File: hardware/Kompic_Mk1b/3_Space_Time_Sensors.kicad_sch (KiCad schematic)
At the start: 37 parts, among them CN1 Qvar_Electrode_2, U5 LSM6DSV16XTR, U6 MAX-M10S-00B, U7 LIS3MDLTR, U8 PCF85063ATL/1,118, X1 FC31M2-32.768-NTLLLDT

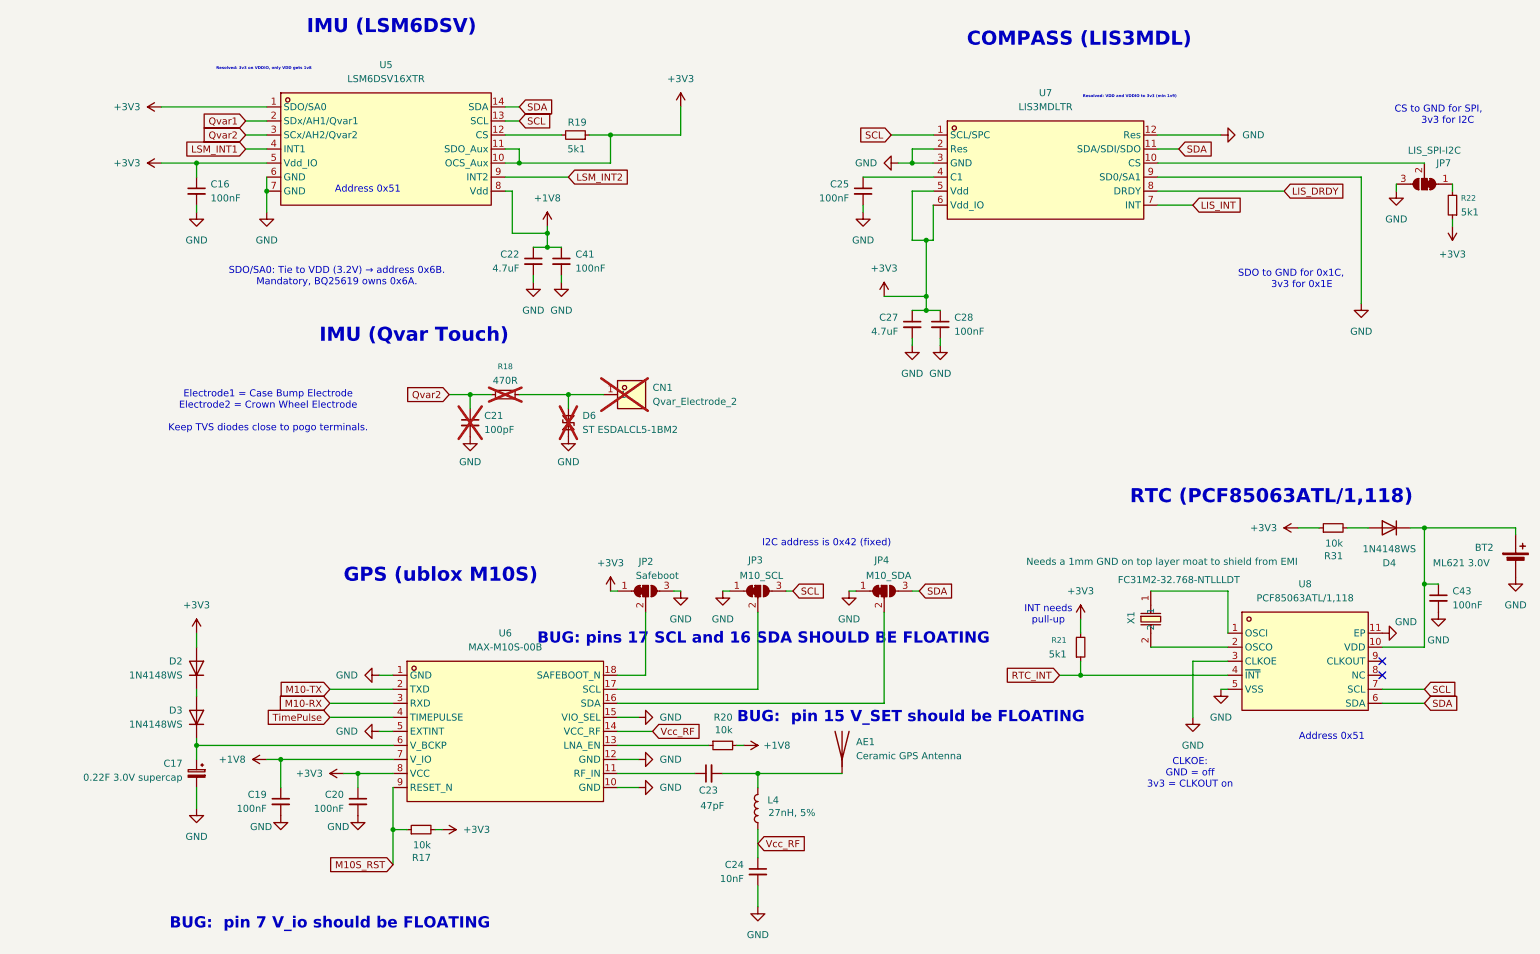
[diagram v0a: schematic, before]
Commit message: Final firmware changes; GPS hardware fixing and arduino sketches (18, 19); Started progress on migrating to LVGL 9 optimized architecture.
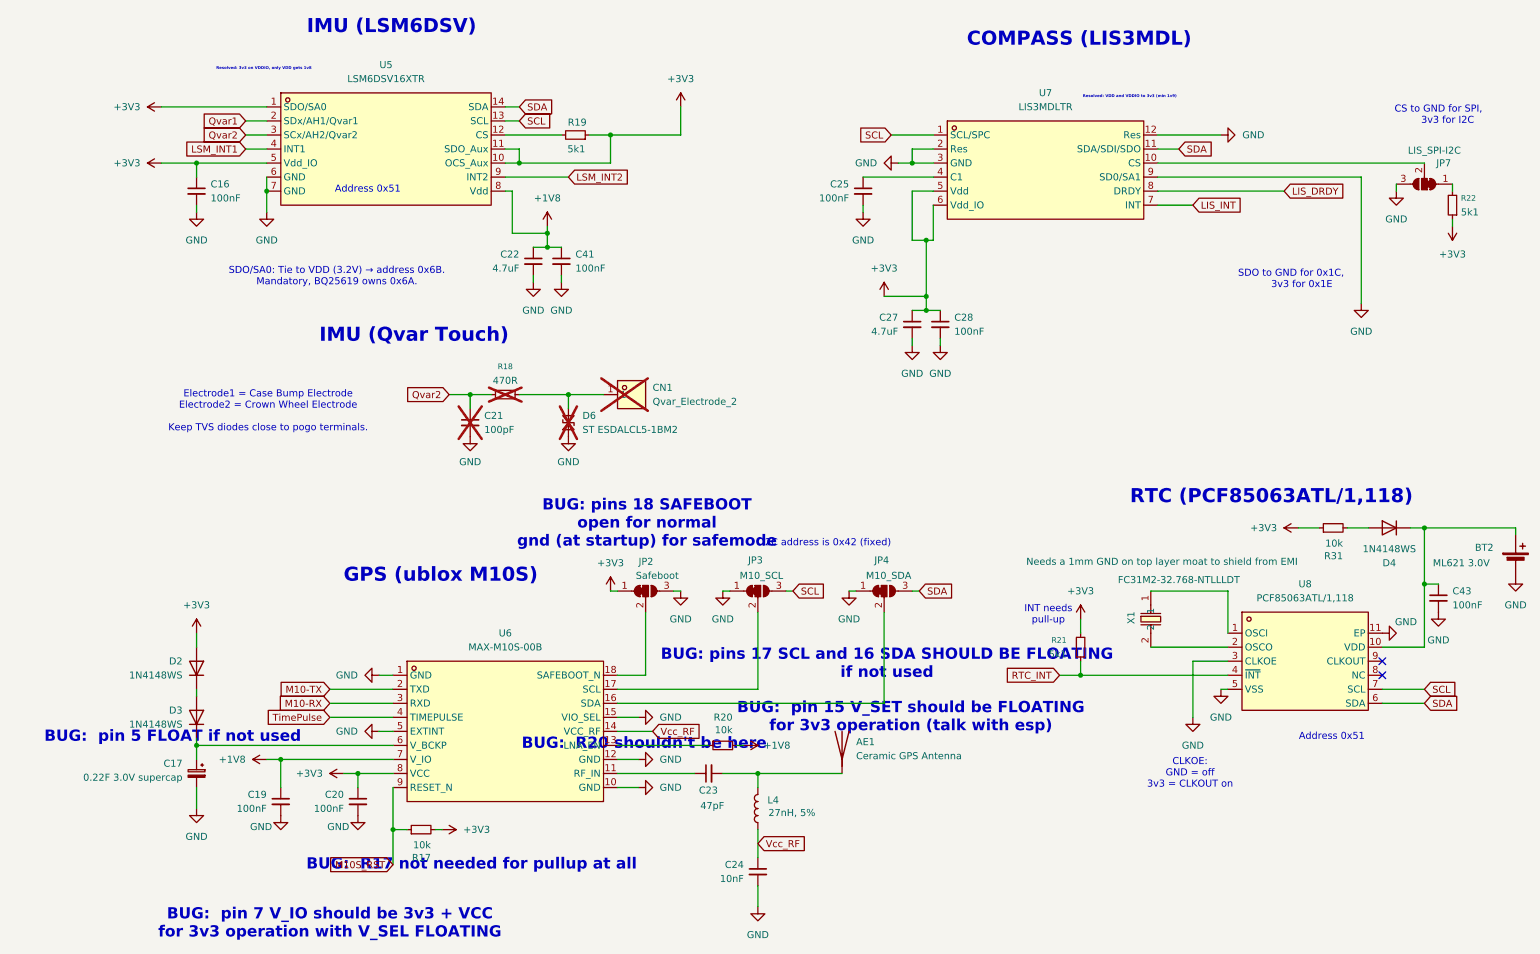
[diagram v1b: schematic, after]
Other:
- note added: "BUG: R17 not needed for pullup at all"
- note added: "BUG: R20 shouldn't be here"
- note added: "BUG: pin 15 V_SET should be FLOATING for 3v3 operation (talk with esp)"
- note added: "BUG: pin 5 FLOAT if not used"
- note added: "BUG: pin 7 V_IO should be 3v3 + VCC for 3v3 operation with V_SEL FLOATING"
- note added: "BUG: pins 17 SCL and 16 SDA SHOULD BE FLOATING if not used"
- note added: "BUG: pins 18 SAFEBOOT open for normal gnd (at startup) for safemode"
- note removed: "BUG: pin 15 V_SET should be FLOATING"
- note removed: "BUG: pin 7 V_io should be FLOATING"
- note removed: "BUG: pins 17 SCL and 16 SDA SHOULD BE FLOATING"
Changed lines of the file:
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@@
 		)
 	)
-	(text "BUG:  pin 7 V_io should be FLOATING"
+	(text "BUG:  pin 7 V_IO should be 3v3 + VCC\nfor 3v3 operation with V_SEL FLOATING"
 		(exclude_from_sim no)
 		(at 62.23 185.928 0)
@@
 		)
 	)
+	(text "BUG:  R20 shouldn't be here"
+		(exclude_from_sim no)
+		(at 119.126 153.416 0)
+		(effects
+			(font
+				(size 2.032 2.032)
+				(thickness 0.4064)
+				(bold yes)
+				(color 255 31 41 1)
+			)
+		)
+	)
 	(text "IMU (Qvar Touch)"
 		(exclude_from_sim no)
@@
 		)
 	)
-	(text "BUG:  pin 15 V_SET should be FLOATING"
+	(text "BUG:  pin 15 V_SET should be FLOATING\nfor 3v3 operation (talk with esp)"
 		(exclude_from_sim no)
 		(at 167.386 148.59 0)
@@
 		)
 	)
-	(text "BUG: pins 17 SCL and 16 SDA SHOULD BE FLOATING"
+	(text "BUG:  R17 not needed for pullup at all"
 		(exclude_from_sim no)
-		(at 140.716 134.366 0)
+		(at 87.884 175.26 0)
+		(effects
+			(font
+				(size 2.032 2.032)
+				(thickness 0.4064)
+				(bold yes)
+				(color 255 31 41 1)
+			)
+		)
+	)
+	(text "BUG: pins 17 SCL and 16 SDA SHOULD BE FLOATING\nif not used"
+		(exclude_from_sim no)
+		(at 163.068 138.938 0)
 		(effects
 			(font
@@
 			)
 		)
+	)
+	(text "BUG:  pin 5 FLOAT if not used"
+		(exclude_from_sim no)
+		(at 33.782 152.146 0)
+		(effects
+			(font
+				(size 2.032 2.032)
+				(thickness 0.4064)
+				(bold yes)
+				(color 255 31 41 1)
+			)
+		)
+	)
+	(text "BUG: pins 18 SAFEBOOT\nopen for normal\ngnd (at startup) for safemode"
+		(exclude_from_sim no)
+		(at 119.634 113.538 0)
+		(effects
+			(font
+				(size 2.032 2.032)
+				(thickness 0.4064)
+				(bold yes)
+				(color 255 31 41 1)
+			)
+		)
